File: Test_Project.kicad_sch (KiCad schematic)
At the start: 51 parts, among them J2 Conn_01x02, J3 Conn_01x03, Q1 Q_NMOS_DSG, Q2 Q_NMOS_DSG, Q3 Q_NMOS_DSG, Q4 Q_NMOS_DSG, U1 STM32L081KZTx, U2 MIC2132YML

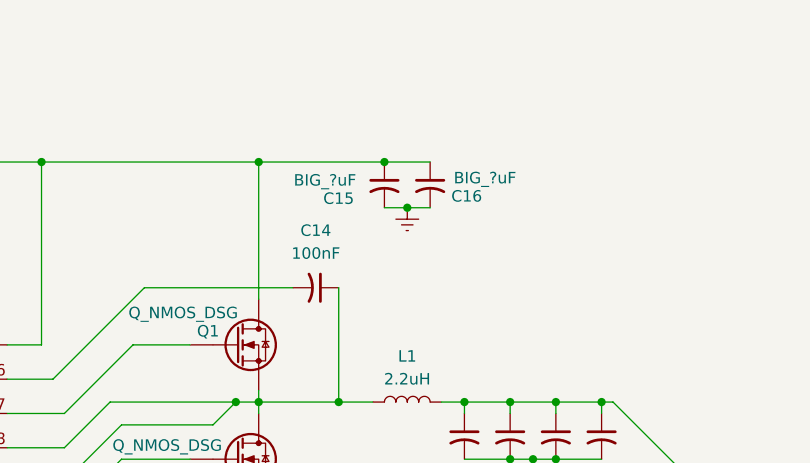
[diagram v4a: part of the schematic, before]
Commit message: Added values to the input decoupling capacitors on the top set of fets
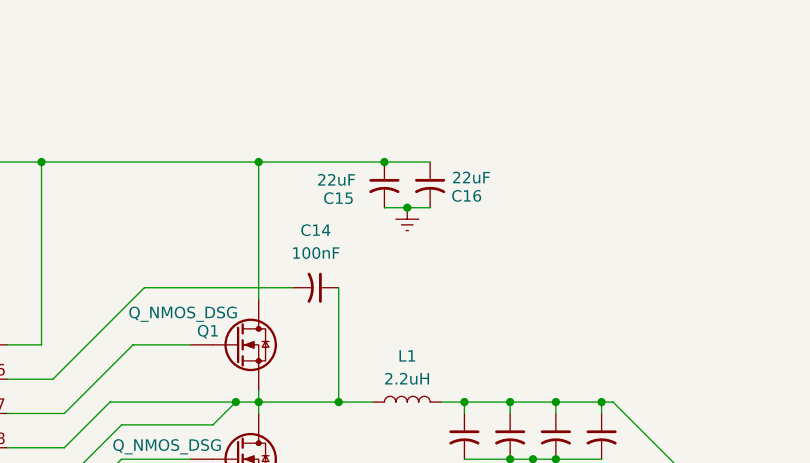
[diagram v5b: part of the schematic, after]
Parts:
- C15, C16: value BIG_?uF -> 22uF
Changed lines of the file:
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@@
 			)
 		)
-		(property "Value" "BIG_?uF"
-			(at 227.076 30.988 0)
+		(property "Value" "22uF"
+			(at 225.552 30.988 0)
 			(effects
 				(font
@@
 			)
 		)
-		(property "Value" "BIG_?uF"
-			(at 209.296 31.242 0)
-			(effects
-				(font
+		(property "Value" "22uF"
+			(at 210.566 31.242 0)
+			(effects
+				(font

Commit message: Finished up schematic
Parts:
- added C28: 100nF, Capacitor_SMD:C_0603_1608Metric_Pad1.08x0.95mm_HandSolder, symbol Library:C_Small_US
- added C29, C30, C31, C32: 1uF, Capacitor_SMD:C_0603_1608Metric_Pad1.08x0.95mm_HandSolder, symbol Library:C_Small_US
- added J4: Conn_01x03, Connector_PinHeader_2.54mm:PinHeader_1x03_P2.54mm_Vertical, symbol Library:Conn_01x03
- added J5, J6: Conn_01x04, Connector_PinHeader_2.54mm:PinHeader_1x04_P2.54mm_Vertical, symbol Library:Conn_01x04
- added Q5: Q_NMOS_DSG, symbol Library:Q_NMOS_DSG_3
- added R15, R18, R19: 25.5 kΩ, Resistor_SMD:R_0805_2012Metric_Pad1.20x1.40mm_HandSolder, symbol Library:R_Small
- added R16, R17: 10k, Resistor_SMD:R_0805_2012Metric_Pad1.20x1.40mm_HandSolder, symbol Library:R_Small
- added R8: 100k, Resistor_SMD:R_0805_2012Metric_Pad1.20x1.40mm_HandSolder, symbol Library:R_Small
- added U3: ~, Package_TO_SOT_SMD:SOT-23W_Handsoldering, symbol Library:AP2127N-3.3
- J2: symbol Connector_Generic:Conn_01x02 -> Library:Conn_01x02
- J3: symbol Connector_Generic:Conn_01x03 -> Library:Conn_01x03
- L1, L2: symbol Device:L -> Library:L
- Q1: symbol Transistor_FET:Q_NMOS_DSG -> Library:Q_NMOS_DSG_1
- Q2: symbol Transistor_FET:Q_NMOS_DSG -> Library:Q_NMOS_DSG_2
- Q3: symbol Transistor_FET:Q_NMOS_DSG -> Library:Q_NMOS_DSG
- Q4: symbol Transistor_FET:Q_NMOS_DSG -> Library:Q_NMOS_DSG_3
- R1: value 10k -> 100k
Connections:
- net LED_Data_Out (PWM): now also Q5.2 (S), R18.1
- net SPI_MISO: now also J5.2 (Pin_2)
- net SPI_MOSI: now also J5.3 (Pin_3)
- net SPI_SCK: now also J5.1 (Pin_1)
- net USART_RX: now also J4.2 (Pin_2)
- net USART_TX: now also J4.1 (Pin_1)
- net VDD_3V3: now also C28.1, C30.1, J6.1 (Pin_1), Q5.3 (G), R18.2, U3.2 (VO)
- net VDD_5V: now also C29.1, U3.3 (VI)
- net Vin: now also R8.2
- net Vout: now also R15.2, R19.2
- net Boot0: now reaches R1.1, U1.31 (BOOT0)
- net I2C_SCL: now reaches U1.29 (PB6)
- net I2C_SCL: now also J6.2 (Pin_2)
- net I2C_SDA: now reaches U1.30 (PB7)
- net I2C_SDA: now also J6.3 (Pin_3)
- net nRST: now reaches C1.1, U1.4 (NRST)
- net GNDREF: no longer names the net of C2.2, C3.2, C4.2, C5.2
- new net: C28.2, C30.2
- new net: C32.1, R15.1, R17.2
- new net: C32.2, R17.1
- new net: Q5.1 (D), R19.1
- new net: C31.1, R16.2, R8.1
- new net: C31.2, R16.1
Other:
- note added: "*Verify LDO footprint before going for it"
- moved on the sheet: J3

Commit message: Added part number for transistors. Need to create footprint and reconsider R_{ILIM}
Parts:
- Q1, Q2, Q3, Q4: value Q_NMOS_DSG -> NTTFS5C454NLTAG
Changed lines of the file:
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@@
 			)
 		)
-		(property "Value" "Q_NMOS_DSG"
-			(at 185.166 76.2 0)
+		(property "Value" "NTTFS5C454NLTAG"
+			(at 190.754 74.93 0)
 			(effects
 				(font
-					(size 1.27 1.27)
+					(size 0.635 0.635)
 				)
 				(justify left)
@@
 			)
 		)
-		(property "Value" "Q_NMOS_DSG"
-			(at 185.674 60.706 0)
+		(property "Value" "NTTFS5C454NLTAG"
+			(at 191.262 59.436 0)
 			(effects
 				(font
-					(size 1.27 1.27)
+					(size 0.635 0.635)
 				)
 				(justify left)
@@
 			)
 		)
-		(property "Value" "Q_NMOS_DSG"
-			(at 185.674 90.678 0)
+		(property "Value" "NTTFS5C454NLTAG"
+			(at 188.976 90.678 0)
 			(effects
 				(font
-					(size 1.27 1.27)
+					(size 0.635 0.635)
 				)
 				(justify left)
@@
 			)
 		)
-		(property "Value" "Q_NMOS_DSG"
-			(at 187.452 45.974 0)
+		(property "Value" "NTTFS5C454NLTAG"
+			(at 193.04 44.704 0)
 			(effects
 				(font
-					(size 1.27 1.27)
+					(size 0.635 0.635)
 				)
 				(justify left)

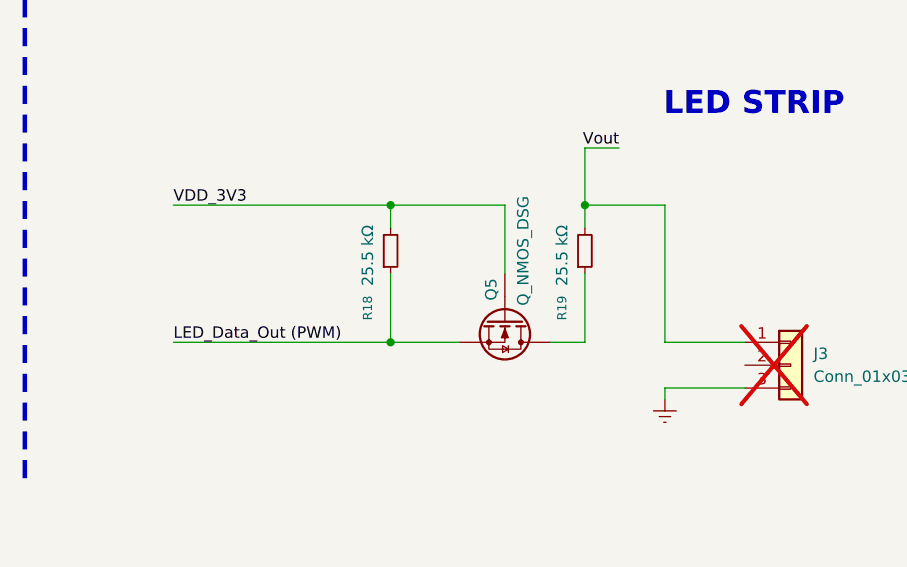
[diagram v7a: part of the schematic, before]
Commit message: Added preliminary footprint for the MOSFETs
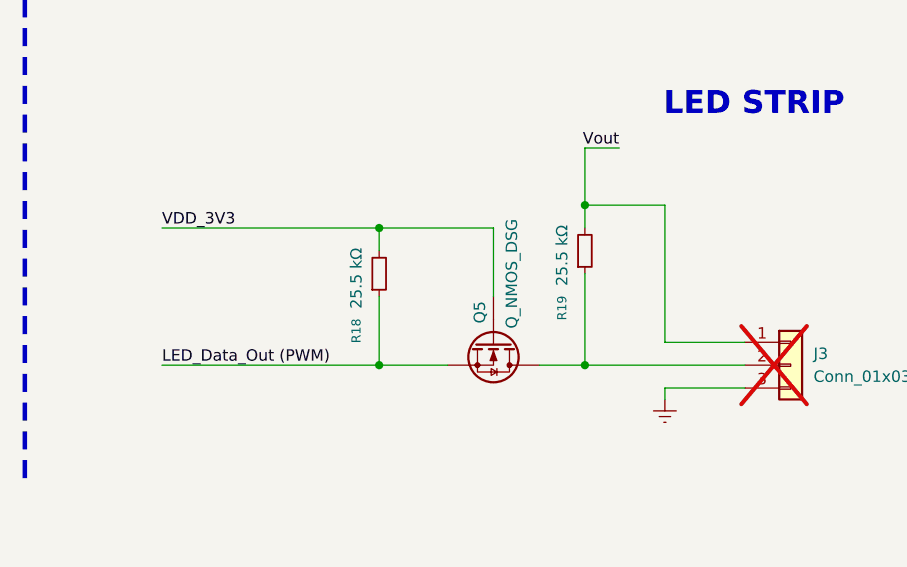
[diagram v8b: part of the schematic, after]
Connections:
- net at J3.2 (Pin_2): now also Q5.1 (D), R19.1
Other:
- moved on the sheet: Q5, R18
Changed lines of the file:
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@@
 	)
 	(junction
+		(at 240.03 152.4)
+		(diameter 0)
+		(color 0 0 0 0)
+	)
+	(junction
 		(at 49.53 134.62)
 		(diameter 0)
@@
 	)
 	(junction
-		(at 218.44 149.86)
+		(at 217.17 152.4)
 		(diameter 0)
 		(color 0 0 0 0)
@@
 	)
 	(junction
-		(at 218.44 134.62)
+		(at 217.17 137.16)
 		(diameter 0)
 		(color 0 0 0 0)
@@
 	(wire
 		(pts
-			(xy 236.22 149.86) (xy 240.03 149.86)
+			(xy 234.95 152.4) (xy 240.03 152.4)
 		)
 		(stroke
@@
 	(wire
 		(pts
-			(xy 240.03 142.24) (xy 240.03 149.86)
+			(xy 240.03 142.24) (xy 240.03 152.4)
 		)
 		(stroke
@@
 	(wire
 		(pts
-			(xy 194.31 134.62) (xy 218.44 134.62)
+			(xy 193.04 137.16) (xy 217.17 137.16)
 		)
 		(stroke
@@
 	(wire
 		(pts
-			(xy 218.44 142.24) (xy 218.44 149.86)
+			(xy 217.17 144.78) (xy 217.17 152.4)
 		)
 		(stroke
@@
 	(wire
 		(pts
-			(xy 218.44 137.16) (xy 218.44 134.62)
+			(xy 217.17 139.7) (xy 217.17 137.16)
 		)
 		(stroke
@@
 	(wire
 		(pts
-			(xy 231.14 134.62) (xy 231.14 142.24)
+			(xy 229.87 137.16) (xy 229.87 144.78)
 		)
 		(stroke
@@
 	(wire
 		(pts
-			(xy 194.31 149.86) (xy 218.44 149.86)
+			(xy 193.04 152.4) (xy 217.17 152.4)
 		)
 		(stroke
@@
 	(wire
 		(pts
-			(xy 218.44 134.62) (xy 231.14 134.62)
+			(xy 217.17 137.16) (xy 229.87 137.16)
 		)
 		(stroke
@@
 	(wire
 		(pts
-			(xy 218.44 149.86) (xy 226.06 149.86)
+			(xy 217.17 152.4) (xy 224.79 152.4)
 		)
 		(stroke
@@
 	(wire
 		(pts
+			(xy 240.03 152.4) (xy 257.81 152.4)
+		)
+		(stroke
+			(width 0)
+			(type default)
+		)
+	)
+	(wire
+		(pts
 			(xy 178.3773 96.5122) (xy 179.6473 96.5122)
 		)
@@
 	)
 	(label "VDD_3V3"
-		(at 194.31 134.62 0)
+		(at 193.04 137.16 0)
 		(effects
 			(font
@@
 	)
 	(label "LED_Data_Out (PWM)"
-		(at 194.31 149.86 0)
+		(at 193.04 152.4 0)
 		(effects
 			(font
@@
 	(symbol
 		(lib_id "Library:R_Small")
-		(at 218.44 139.7 0)
+		(at 217.17 142.24 0)
 		(mirror x)
 		(unit 1)
@@
 		(dnp no)
 		(property "Reference" "R18"
-			(at 215.9 146.05 90)
+			(at 214.63 148.59 90)
 			(effects
 				(font
@@
 		)
 		(property "Value" "25.5 kΩ"
-			(at 215.9 140.208 90)
+			(at 214.63 142.748 90)
 			(effects
 				(font
@@
 		)
 		(property "Footprint" "Resistor_SMD:R_0805_2012Metric_Pad1.20x1.40mm_HandSolder"
-			(at 218.44 139.7 0)
+			(at 217.17 142.24 0)
 			(effects
 				(font
@@
 		)
 		(property "Datasheet" "~"
-			(at 218.44 139.7 0)
+			(at 217.17 142.24 0)
 			(effects
 				(font
@@
 		)
 		(property "Description" "Resistor, small symbol"
-			(at 218.44 139.7 0)
+			(at 217.17 142.24 0)
 			(effects
 				(font
@@
 		(lib_name "Q_NMOS_DSG_3")
 		(lib_id "Library:Q_NMOS_DSG_3")
-		(at 231.14 147.32 270)
+		(at 229.87 149.86 270)
 		(unit 1)
 		(exclude_from_sim no)
@@
 		(dnp no)
 		(property "Reference" "Q5"
-			(at 229.616 142.748 0)
+			(at 228.346 145.288 0)
 			(effects
 				(font
@@
 		)
 		(property "Value" "Q_NMOS_DSG"
-			(at 233.172 133.604 0)
+			(at 231.902 136.144 0)
 			(effects
 				(font
@@
 		)
 		(property "Footprint" ""
-			(at 233.68 152.4 0)
+			(at 232.41 154.94 0)
 			(effects
 				(font
@@
 		)
 		(property "Datasheet" "~"
-			(at 231.14 147.32 0)
+			(at 229.87 149.86 0)
 			(effects
 				(font
@@
 		)
 		(property "Description" "N-MOSFET transistor, drain/source/gate"
-			(at 231.14 147.32 0)
+			(at 229.87 149.86 0)
 			(effects
 				(font
